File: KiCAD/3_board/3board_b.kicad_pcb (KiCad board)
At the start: 2 copper layers, 92.5 x 89.5 mm, 29 parts, among them SW10_SHARE SW_Push, SW11_START SW_Push, SW14_PS SW_Push, SW15_TOUCHPAD SW_Push, SW2_LK SW_Push, SW3_MK SW_Push, SW4_LP SW_Push, SW5_MP SW_Push, SW6_DI SW_Push, SW7_HP SW_Push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

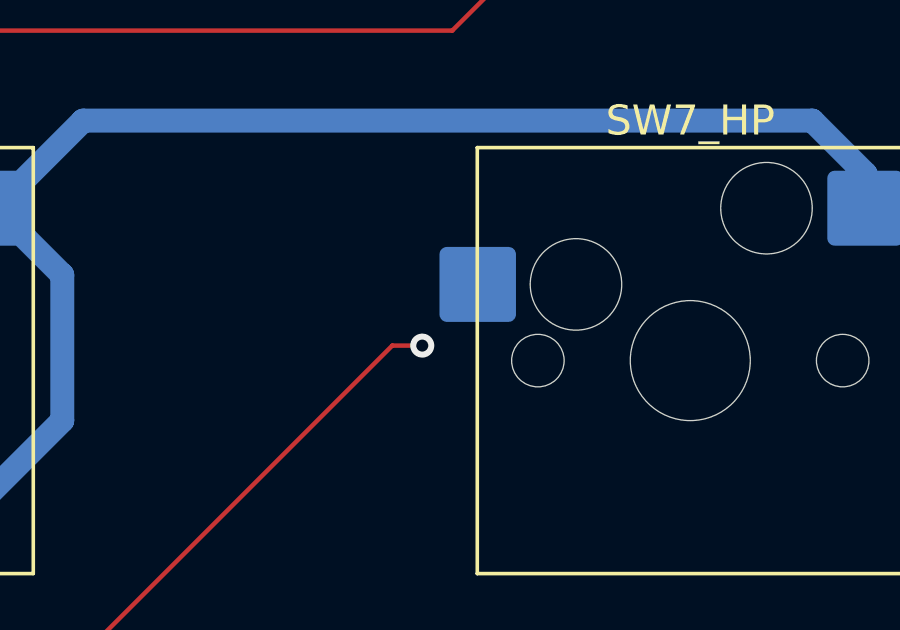
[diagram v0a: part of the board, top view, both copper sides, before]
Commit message: Fix missing connection to HP
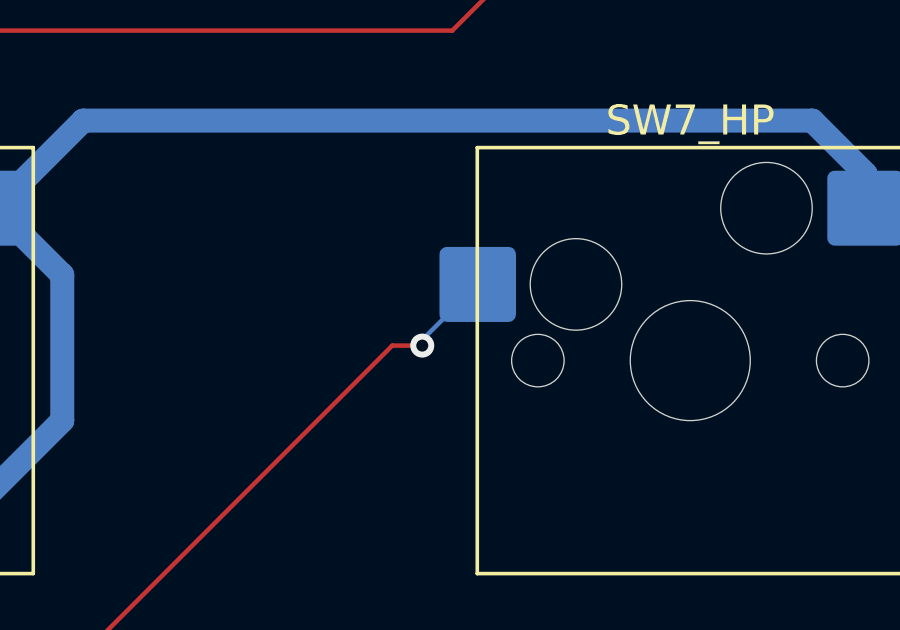
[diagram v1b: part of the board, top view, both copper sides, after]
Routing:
- net /Buttons/R1: track 78.3 -> 81.1 mm
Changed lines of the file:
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@@
+	)
+	(segment
+		(start 162.235 54.308943)
+		(end 164.083943 52.46)
+		(width 0.15)
+		(layer "B.Cu")
+		(net 7)
+	)
+	(segment
+		(start 162.235 54.5)
+		(end 162.235 54.308943)
+		(width 0.15)
+		(layer "B.Cu")
+		(net 7)
 	)
 	(segment
